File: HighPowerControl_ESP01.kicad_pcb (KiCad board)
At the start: 2 copper layers, 70 x 45 mm, 9 parts, among them J1 AC Input, J2 ESP-01, J3 AMS1117Module, J4 To SSR

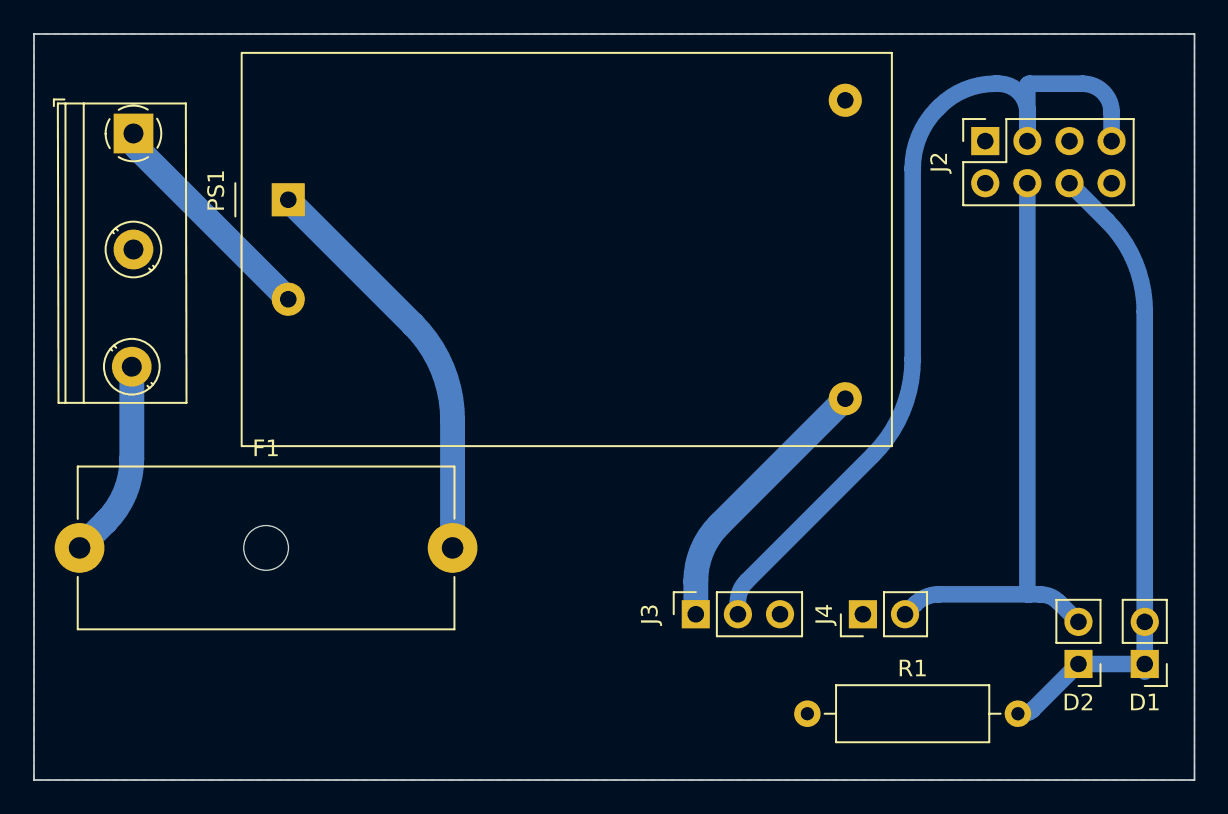
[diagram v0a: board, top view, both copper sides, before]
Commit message: Flip the HiLInk AC-DC converter footprint
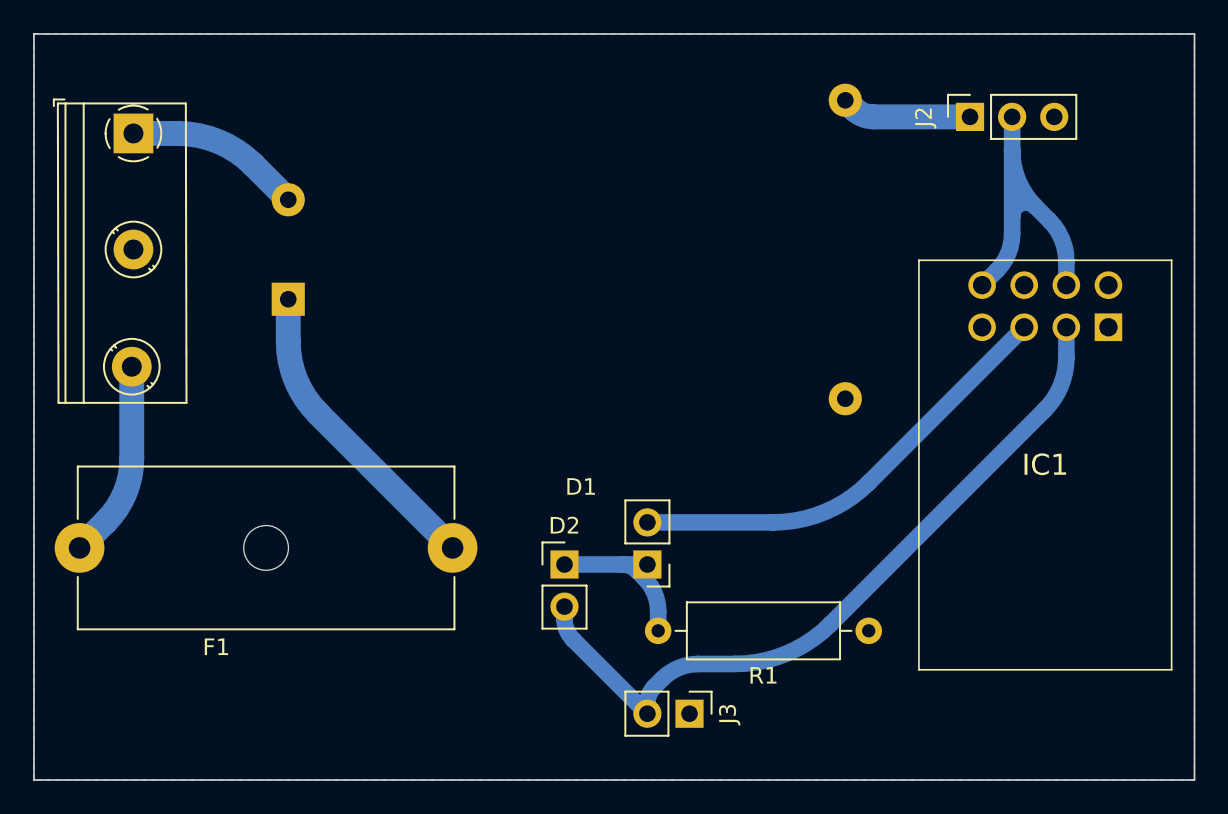
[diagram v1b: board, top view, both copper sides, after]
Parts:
- removed J4: To SSR, Connector_PinHeader_2.54mm:PinHeader_1x02_P2.54mm_Vertical
- added IC1: ESP-01, ESP-01:ESP01, F.Cu at (84.8, 37.7)
- J2: value ESP-01 -> AMS1117Module; footprint Connector_PinSocket_2.54mm:PinSocket_2x04_P2.54mm_Vertical -> Connector_PinSocket_2.54mm:PinSocket_1x03_P2.54mm_Vertical
- J3: value AMS1117Module -> To SSR; footprint Connector_PinSocket_2.54mm:PinSocket_1x03_P2.54mm_Vertical -> Connector_PinHeader_2.54mm:PinHeader_1x02_P2.54mm_Vertical
- PS1: moved to B.Cu
- moved D2 31.6 mm to (52.0, 52.0), turned to 0 degrees
- moved D1 30.6 mm to (57.0, 52.0)
- moved R1 6.22 mm to (70.3, 56.0), turned to 180 degrees
- moved J3 6.01 mm to (59.5, 61.0), turned to -90 degrees
- moved PS1 6.00 mm to (35.3, 36.0)
- moved J2 1.73 mm to (76.5, 25.0)
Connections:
- J2 pad 1: unconnected-(J2-Pin_1-Pad1) -> /5V
- J2 pad 2: GND -> /3V3
- J2 pad 3: /3V3 -> /GndL
- J3 pad 1: /5V -> /GndL
- J3 pad 2: /3V3 -> /Relay
- PS1 pad 3: GND -> /GndL
- R1 pad 1: GND -> /GndL
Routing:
- net /3V3: track 54.4 -> 21.7 mm
- net /5V: track 16.5 -> 7.85 mm
- net /Relay: track 36.4 -> 44.8 mm
- net Net-(PS1-AC/L): track 24.7 -> 18.8 mm
- net /LED: track 31.0 -> 27.2 mm
- net /AC_N: track 13.8 -> 10.9 mm
- net Net-(D1-K): track 8.85 -> 10.5 mm
- added copper zone on B.Cu, net /GndL
- removed copper zone on B.Cu, net GND

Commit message: Inverting logic of SSR
when SSR is connected to the GPIO it causes an issue in the boot of ESP-01
So the circuit was changed slightly based on the suggestions  in https://arduino.stackexchange.com/questions/37303/esp8266-esp-01-not-booting-with-load-on-io-pin-2
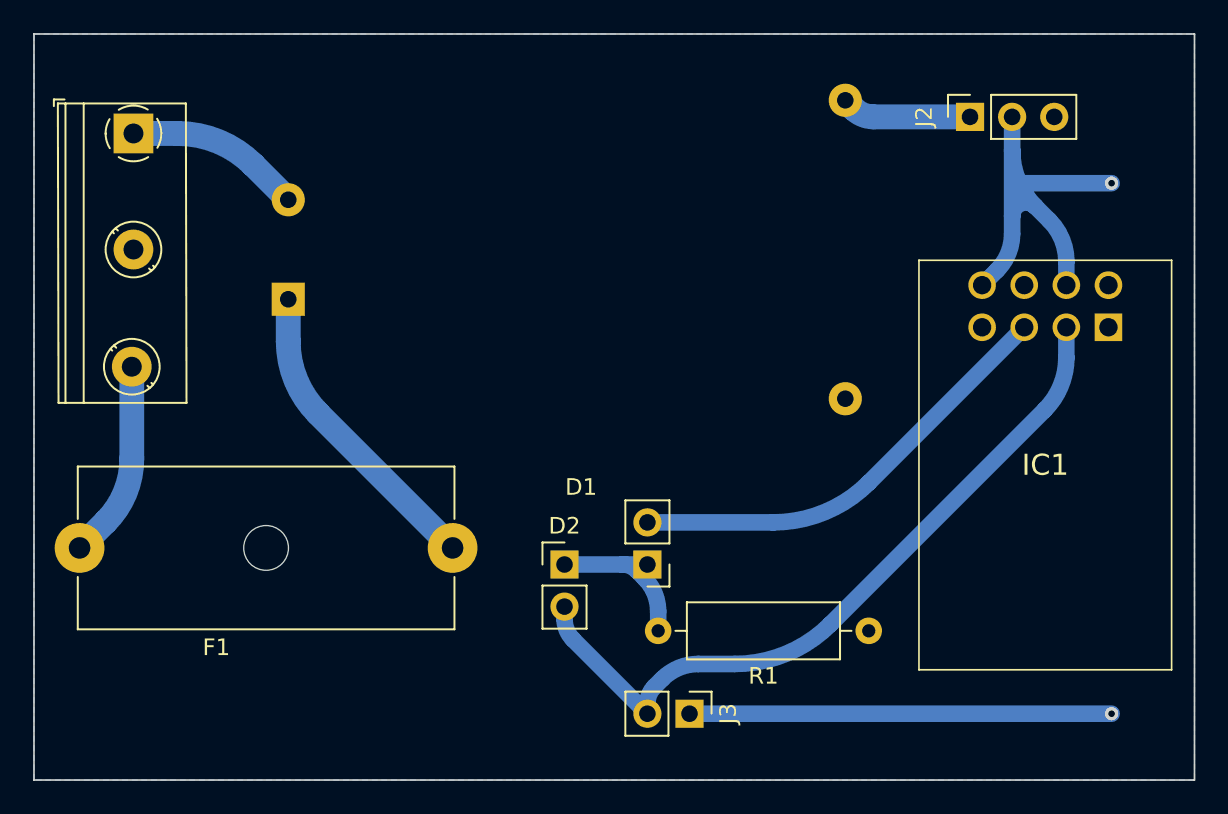
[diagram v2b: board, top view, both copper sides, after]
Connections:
- J3 pad 1: /GndL -> /3V3
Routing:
- net /3V3: track 21.7 -> 52.7 mm, vias 0 -> 2
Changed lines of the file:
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@@
       (stroke (width 0.1) (type solid)) (layer "F.Fab"))
     (pad "1" thru_hole rect (at 0 0 270) (size 1.7 1.7) (drill 1) (layers "*.Cu" "*.Mask")
-      (net 6 "/GndL") (pinfunction "Pin_1") (pintype "passive"))
+      (net 7 "/3V3") (pinfunction "Pin_1") (pintype "passive"))
     (pad "2" thru_hole oval (at 0 2.54 270) (size 1.7 1.7) (drill 1) (layers "*.Cu" "*.Mask")
       (net 3 "/Relay") (pinfunction "Pin_2") (pintype "passive"))
@@
   (segment (start 37.136202 42.886202) (end 45.25 51) (width 1.5) (layer "B.Cu") (net 4))
   (segment (start 35.3375 38.54375) (end 35.3375 36) (width 1.5) (layer "B.Cu") (net 4))
-  (arc (start 35.3375 38.54375) (mid 35.804967 40.893868) (end 37.136202 42.886202) (width 1.5) (layer "B.Cu") (net 4))
-  (segment (start 79 31) (end 79 27) (width 1) (layer "B.Cu") (net 7))
-  (segment (start 80.414213 30.414213) (end 81.251766 31.251766) (width 1) (layer "B.Cu") (net 7))
-  (segment (start 79 31) (end 79 32.060136) (width 1) (layer "B.Cu") (net 7))
+  (arc (start 37.136202 42.886202) (mid 35.804967 40.893868) (end 35.3375 38.54375) (width 1.5) (layer "B.Cu") (net 4))
+  (via (at 85 61) (size 0.8) (drill 0.4) (layers "F.Cu" "B.Cu") (free) (net 7))
+  (via (at 85 29) (size 0.8) (drill 0.4) (layers "F.Cu" "B.Cu") (free) (net 7))
+  (segment (start 85 29) (end 79.433694 29) (width 1) (layer "B.Cu") (net 7))
+  (segment (start 79 27) (end 79 31) (width 1) (layer "B.Cu") (net 7))
+  (segment (start 81.251766 31.251766) (end 80.414213 30.414213) (width 1) (layer "B.Cu") (net 7))
+  (segment (start 79 32.060136) (end 79 31) (width 1) (layer "B.Cu") (net 7))
   (segment (start 82.27 33.71) (end 82.27 35.15) (width 1) (layer "B.Cu") (net 7))
   (segment (start 79 27) (end 79 25) (width 1) (layer "B.Cu") (net 7))
+  (segment (start 85 61) (end 59.54 61) (width 1) (layer "B.Cu") (net 7))
   (segment (start 78.095 34.245) (end 77.19 35.15) (width 1) (layer "B.Cu") (net 7))
   (arc (start 81.251766 31.251766) (mid 82.005369 32.379613) (end 82.27 33.71) (width 1) (layer "B.Cu") (net 7))
   (arc (start 80.414213 30.414213) (mid 79.511401 30.234632) (end 79 31) (width 1) (layer "B.Cu") (net 7))
-  (arc (start 79 32.060136) (mid 78.764798 33.242576) (end 78.095 34.245) (width 1) (layer "B.Cu") (net 7))
-  (arc (start 79 27) (mid 79.367541 28.847758) (end 80.414213 30.414213) (width 1) (layer "B.Cu") (net 7))
+  (arc (start 78.095 34.245) (mid 78.764798 33.242576) (end 79 32.060136) (width 1) (layer "B.Cu") (net 7))
+  (arc (start 80.414213 30.414213) (mid 79.367541 28.847758) (end 79 27) (width 1) (layer "B.Cu") (net 7))
   (segment (start 25.9 45.622613) (end 25.9 40.07) (width 1.5) (layer "B.Cu") (net 8))
   (segment (start 24.325 49.425) (end 22.75 51) (width 1.5) (layer "B.Cu") (net 8))
@@
   (segment (start 26 26.165625) (end 26 26.33125) (width 1.5) (layer "B.Cu") (net 9))
   (arc (start 33.224591 27.887091) (mid 31.134353 26.490438) (end 28.66875 26) (width 1.5) (layer "B.Cu") (net 9))
-  (arc (start 26.165625 26) (mid 26.04851 26.04851) (end 26 26.165625) (width 1.5) (layer "B.Cu") (net 9))
+  (arc (start 26 26.165625) (mid 26.04851 26.04851) (end 26.165625 26) (width 1.5) (layer "B.Cu") (net 9))
   (segment (start 69.4375 24.5) (end 68.9375 24) (width 1.5) (layer "B.Cu") (net 10))
   (segment (start 70.644606 25) (end 76.46 25) (width 1.5) (layer "B.Cu") (net 10))
-  (arc (start 69.4375 24.5) (mid 69.991325 24.870054) (end 70.644606 25) (width 1.5) (layer "B.Cu") (net 10))
+  (arc (start 70.644606 25) (mid 69.991325 24.870054) (end 69.4375 24.5) (width 1.5) (layer "B.Cu") (net 10))
   (zone (net 6) (net_name "/GndL") (layer "B.Cu") (hatch edge 0.5)
     (connect_pads (clearance 1))
